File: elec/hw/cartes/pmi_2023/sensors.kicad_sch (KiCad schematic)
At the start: 51 parts, among them SW1 ESE22MH22, SW2 ESE22MH24, U10 tof_sensor_master, U12 LSM6DSO32XTR, U13 GP2S60B, U14 GP2S60B, U15 GP2S60B, U16 GP2S60B, U17 tof_sensor_master, U19 GP2S60B, U20 GP2S60B, U21 tof_sensor_master, U5 AD8531ARTZ, U6 tof_sensor_master, U7 XRA1200PIG16TR-F, U8 GP2S60B, U9 GP2S60B

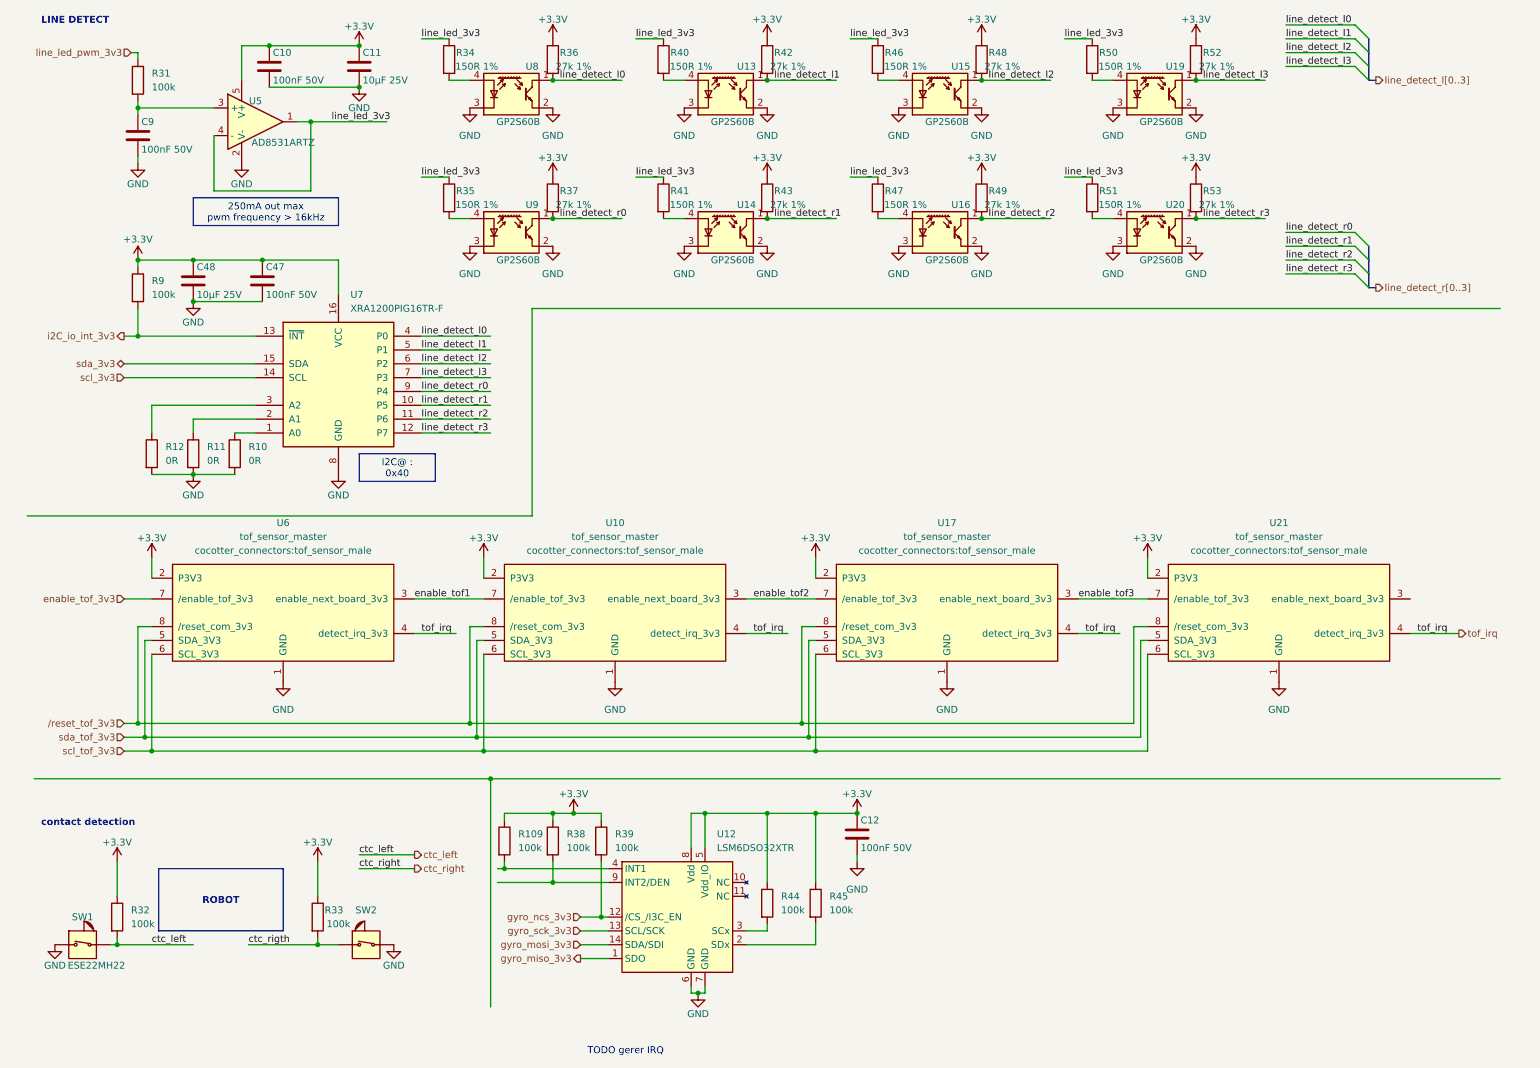
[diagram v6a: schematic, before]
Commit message: pmi layout (WIP)
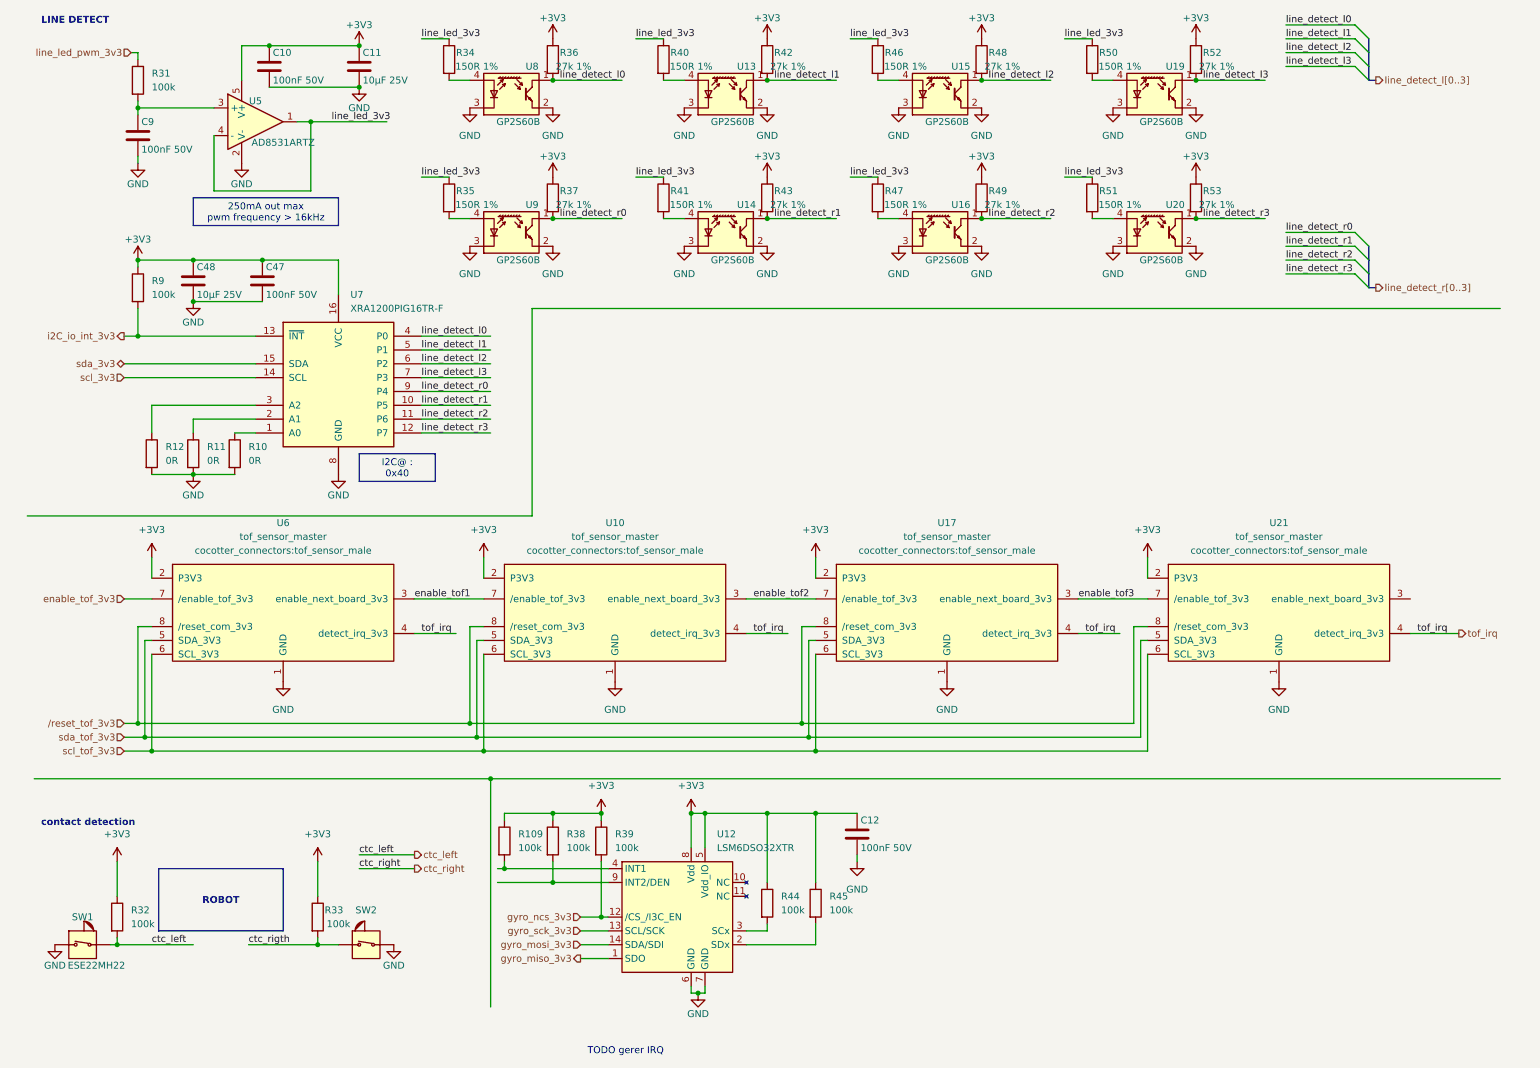
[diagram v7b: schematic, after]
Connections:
- net +3.3V renamed +3V3

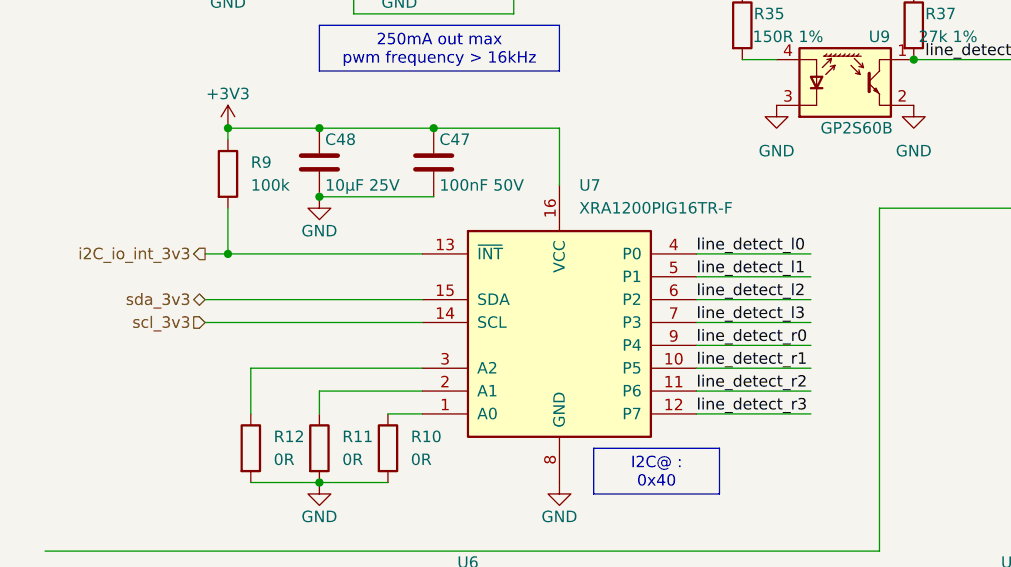
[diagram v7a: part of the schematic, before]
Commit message: pmi layout (WIP)
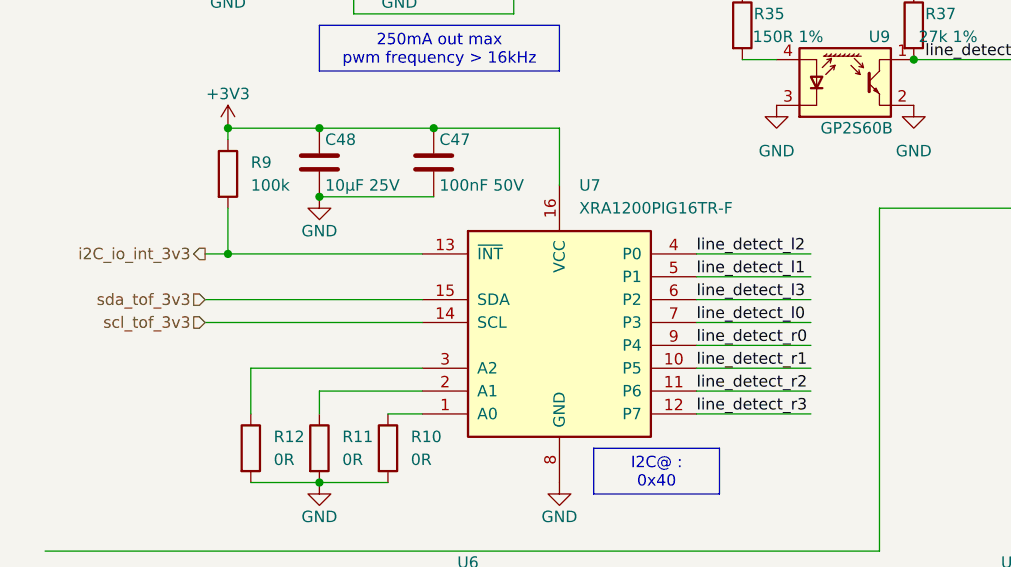
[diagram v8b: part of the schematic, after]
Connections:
- net scl_3v3 is gone; now on net scl_tof_3v3: U7.14 (SCL)
- net sda_3v3 is gone; now on net sda_tof_3v3: U7.15 (SDA)
- net line_detect_l0: now also U7.7 (P3); no longer U7.4 (P0)
- net line_detect_l2: now also U7.4 (P0); no longer U7.6 (P2)
- net line_detect_l3: now also U7.6 (P2); no longer U7.7 (P3)
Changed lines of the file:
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@@
     (effects (font (size 1.27 1.27)) (justify left bottom))
   )
-  (label "line_detect_l0" (at 85.09 72.39 0) (fields_autoplaced)
+  (label "line_detect_l0" (at 85.09 80.01 0) (fields_autoplaced)
     (effects (font (size 1.27 1.27)) (justify left bottom))
   )
@@
     (effects (font (size 1.27 1.27)) (justify left bottom))
   )
-  (label "line_detect_l3" (at 85.09 80.01 0) (fields_autoplaced)
+  (label "line_detect_l3" (at 85.09 77.47 0) (fields_autoplaced)
     (effects (font (size 1.27 1.27)) (justify left bottom))
   )
@@
     (effects (font (size 1.27 1.27)) (justify left bottom))
   )
-  (label "line_detect_l2" (at 85.09 77.47 0) (fields_autoplaced)
+  (label "line_detect_l2" (at 85.09 72.39 0) (fields_autoplaced)
     (effects (font (size 1.27 1.27)) (justify left bottom))
   )
@@
     (effects (font (size 1.27 1.27)) (justify left bottom))
   )
-  (hierarchical_label "scl_3v3" (shape input) (at 30.48 80.01 180) (fields_autoplaced)
+  (hierarchical_label "gyro_sck_3v3" (shape input) (at 114.3 181.61 180) (fields_autoplaced)
     (effects (font (size 1.27 1.27)) (justify right))
   )
-  (hierarchical_label "gyro_sck_3v3" (shape input) (at 114.3 181.61 180) (fields_autoplaced)
+  (hierarchical_label "sda_tof_3v3" (shape input) (at 30.48 77.47 180) (fields_autoplaced)
     (effects (font (size 1.27 1.27)) (justify right))
   )
@@
     (effects (font (size 1.27 1.27)) (justify right))
   )
+  (hierarchical_label "scl_tof_3v3" (shape input) (at 30.48 80.01 180) (fields_autoplaced)
+    (effects (font (size 1.27 1.27)) (justify right))
+  )
   (hierarchical_label "line_detect_r[0..3]" (shape output) (at 260.35 63.5 0) (fields_autoplaced)
     (effects (font (size 1.27 1.27)) (justify left))
@@
     (effects (font (size 1.27 1.27)) (justify right))
   )
-  (hierarchical_label "sda_3v3" (shape bidirectional) (at 30.48 77.47 180) (fields_autoplaced)
-    (effects (font (size 1.27 1.27)) (justify right))
-  )
